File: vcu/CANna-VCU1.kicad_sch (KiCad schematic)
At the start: 12 parts, among them J10 M80-5401042, J11 Conn_01x08_Socket, J12 Conn_01x38_Socket, J13 Conn_01x04_Socket, J14 Conn_01x06_Socket, J3 M80-5401042, J8 M80-5401042, J9 M80-5404242

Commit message: Pfft 3AM changes who knows what this is, probably footprint stuff
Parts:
- J10, J8: footprint (none) -> SUFST:M80-5401042
- J12: footprint (none) -> SUFST:M80-5403842
- J13: footprint (none) -> SUFST:M80-5400442
- J14: footprint (none) -> SUFST:M80-5400642
- J9: footprint (none) -> SUFST:M80-5404242
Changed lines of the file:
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@@
 			)
 		)
-		(property "Footprint" ""
+		(property "Footprint" "SUFST:M80-5404242"
 			(at 177.8 224.79 0)
 			(effects
@@
 			)
 		)
-		(property "Footprint" ""
+		(property "Footprint" "SUFST:M80-5400642"
 			(at 88.9 205.74 0)
 			(effects
@@
 			)
 		)
-		(property "Footprint" ""
+		(property "Footprint" "SUFST:M80-5401042"
 			(at 223.52 189.23 0)
 			(effects
@@
 			)
 		)
-		(property "Footprint" ""
+		(property "Footprint" "SUFST:M80-5401042"
 			(at 53.34 205.74 0)
 			(effects
@@
 			)
 		)
-		(property "Footprint" ""
+		(property "Footprint" "SUFST:M80-5403842"
 			(at 21.59 229.87 0)
 			(effects
@@
 			)
 		)
-		(property "Footprint" ""
+		(property "Footprint" "SUFST:M80-5400442"
 			(at 88.9 248.92 0)
 			(effects

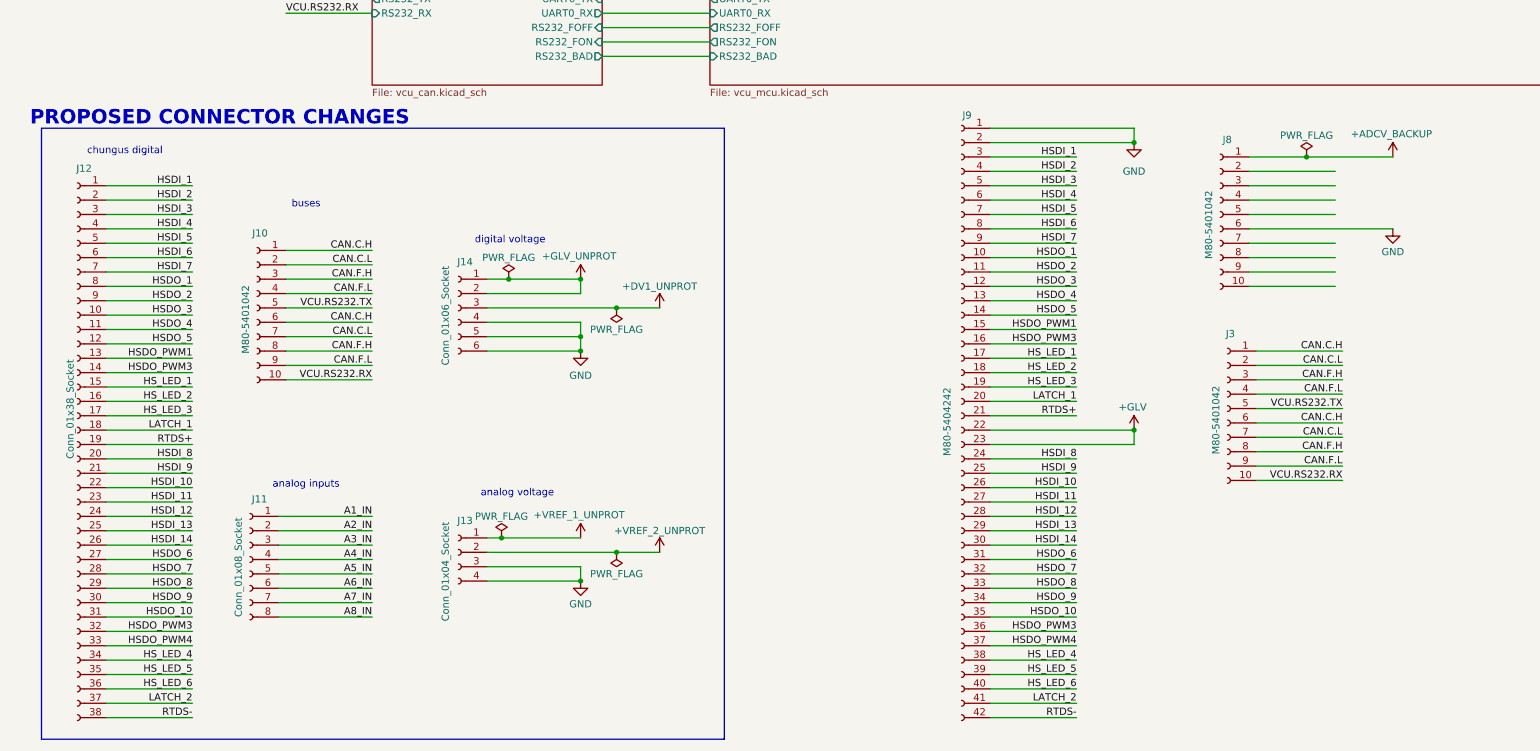
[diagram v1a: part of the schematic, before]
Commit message: fixed connector pinouts
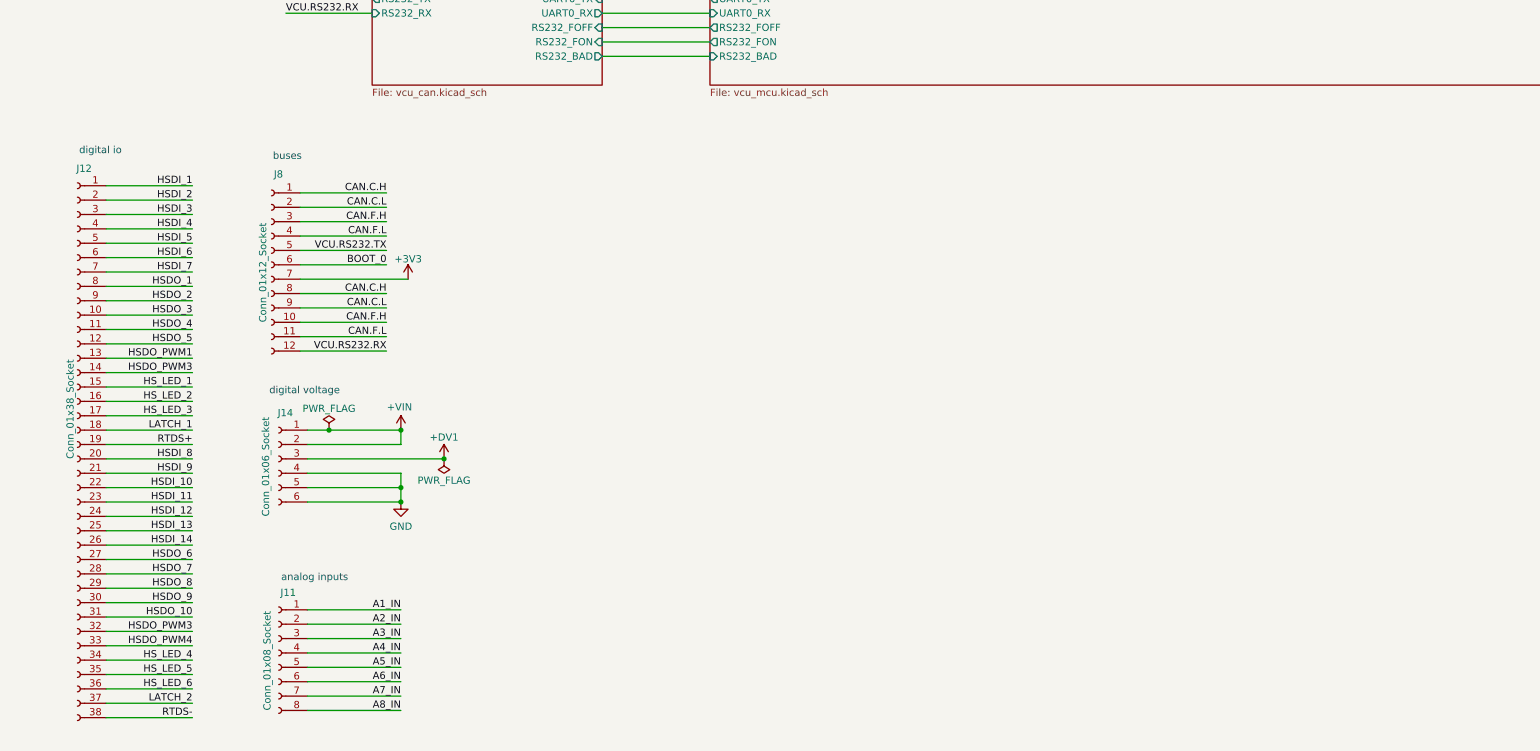
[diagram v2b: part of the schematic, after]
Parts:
- removed J10, J8: M80-5401042, SUFST:M80-5401042, symbol Connector:Conn_01x10_Socket
- removed J13: Conn_01x04_Socket, SUFST:M80-5400442, symbol Connector:Conn_01x04_Socket
- removed J3: M80-5401042, symbol Connector:Conn_01x10_Socket
- removed J9: M80-5404242, SUFST:M80-5404242, symbol Connector:Conn_01x42_Socket
- added J8: Conn_01x12_Socket, symbol Connector:Conn_01x12_Socket
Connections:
- net CAN.C.H: now also J8.1 (Pin_1), J8.8 (Pin_8)
- net CAN.C.L: now also J8.2 (Pin_2), J8.9 (Pin_9)
- net CAN.F.H: now also J8.10 (Pin_10), J8.3 (Pin_3)
- net CAN.F.L: now also J8.11 (Pin_11), J8.4 (Pin_4)
- net VCU.RS232.RX: now also J8.12 (Pin_12)
- net VCU.RS232.TX: now also J8.5 (Pin_5)
- net +DV1_UNPROT renamed +DV1
- net +GLV_UNPROT renamed +VIN
- new net +3V3: J8.7 (Pin_7)
- new net BOOT_0: J8.6 (Pin_6)
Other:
- note added: "digital io"
- note removed: "PROPOSED CONNECTOR CHANGES"
- note removed: "analog voltage"
- note removed: "chungus digital"
- moved on the sheet: J11, J14

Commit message: laying out components
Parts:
- J11: value Conn_01x08_Socket -> M80-5400842; footprint (none) -> SUFST:M80-5400842
- J12: value Conn_01x38_Socket -> M80-5403842
- J14: value Conn_01x06_Socket -> M80-5400642
- J8: value Conn_01x12_Socket -> M80-5401242; footprint (none) -> SUFST:M80-5401242
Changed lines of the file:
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@@
 			)
 		)
-		(property "Value" "Conn_01x12_Socket"
+		(property "Value" "M80-5401242"
 			(at 54.356 208.28 90)
 			(effects
@@
 			)
 		)
-		(property "Footprint" ""
+		(property "Footprint" "SUFST:M80-5401242"
 			(at 55.88 198.12 0)
 			(effects
@@
 			)
 		)
-		(property "Value" "Conn_01x08_Socket"
+		(property "Value" "M80-5400842"
 			(at 55.118 276.86 90)
 			(effects
@@
 			)
 		)
-		(property "Footprint" ""
+		(property "Footprint" "SUFST:M80-5400842"
 			(at 57.15 266.7 0)
 			(effects
@@
 			)
 		)
-		(property "Value" "Conn_01x06_Socket"
+		(property "Value" "M80-5400642"
 			(at 54.864 242.57 90)
 			(effects
@@
 			)
 		)
-		(property "Value" "Conn_01x38_Socket"
+		(property "Value" "M80-5403842"
 			(at 20.32 232.4099 90)
 			(effects

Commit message: layout hell
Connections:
- net HSDO_PWM3: no longer J12.14 (Pin_14)
- new net HSDO_PWM2: J12.14 (Pin_14)

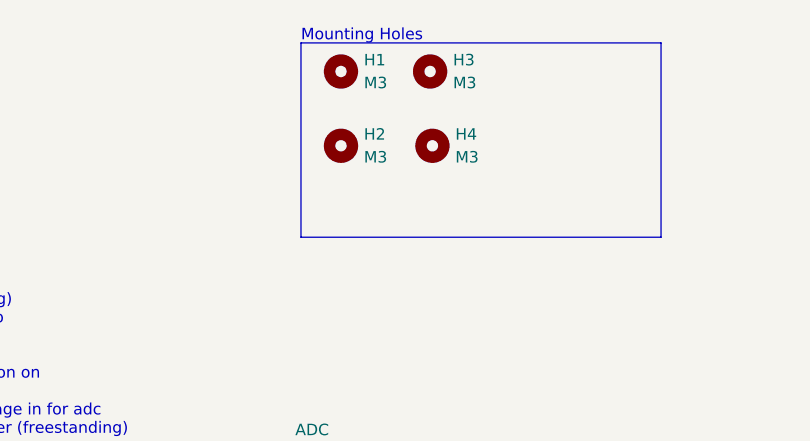
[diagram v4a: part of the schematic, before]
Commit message: added pours
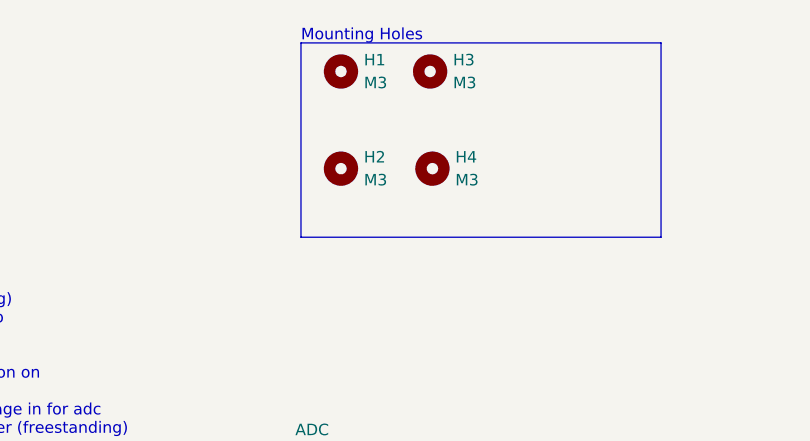
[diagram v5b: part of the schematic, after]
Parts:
- H1, H2, H3, H4: footprint MountingHole:MountingHole_3.2mm_M3 -> MountingHole:MountingHole_3.2mm_M3_DIN965_Pad_TopBottom
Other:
- moved on the sheet: H2, H4
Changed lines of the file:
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@@
 	(symbol
 		(lib_id "Mechanical:MountingHole")
-		(at 88.9 34.29 0)
+		(at 88.9 36.83 0)
 		(unit 1)
 		(exclude_from_sim no)
@@
 		(fields_autoplaced yes)
 		(property "Reference" "H4"
-			(at 91.44 33.0199 0)
+			(at 91.44 35.5599 0)
 			(effects
 				(font
@@
 		)
 		(property "Value" "M3"
-			(at 91.44 35.5599 0)
-			(effects
-				(font
-					(size 1.27 1.27)
-				)
-				(justify left)
-			)
-		)
-		(property "Footprint" "MountingHole:MountingHole_3.2mm_M3"
-			(at 88.9 34.29 0)
+			(at 91.44 38.0999 0)
+			(effects
+				(font
+					(size 1.27 1.27)
+				)
+				(justify left)
+			)
+		)
+		(property "Footprint" "MountingHole:MountingHole_3.2mm_M3_DIN965_Pad_TopBottom"
+			(at 88.9 36.83 0)
 			(effects
 				(font
@@
 		)
 		(property "Datasheet" "~"
-			(at 88.9 34.29 0)
+			(at 88.9 36.83 0)
 			(effects
 				(font
@@
 		)
 		(property "Description" ""
-			(at 88.9 34.29 0)
+			(at 88.9 36.83 0)
 			(effects
 				(font
@@
 		)
 		(property "Optional" "False"
-			(at 88.9 34.29 0)
+			(at 88.9 36.83 0)
 			(effects
 				(font
@@
 	(symbol
 		(lib_id "Mechanical:MountingHole")
-		(at 78.74 34.29 0)
+		(at 78.74 36.83 0)
 		(unit 1)
 		(exclude_from_sim no)
@@
 		(fields_autoplaced yes)
 		(property "Reference" "H2"
-			(at 81.28 33.0199 0)
+			(at 81.28 35.5599 0)
 			(effects
 				(font
@@
 		)
 		(property "Value" "M3"
-			(at 81.28 35.5599 0)
-			(effects
-				(font
-					(size 1.27 1.27)
-				)
-				(justify left)
-			)
-		)
-		(property "Footprint" "MountingHole:MountingHole_3.2mm_M3"
-			(at 78.74 34.29 0)
+			(at 81.28 38.0999 0)
+			(effects
+				(font
+					(size 1.27 1.27)
+				)
+				(justify left)
+			)
+		)
+		(property "Footprint" "MountingHole:MountingHole_3.2mm_M3_DIN965_Pad_TopBottom"
+			(at 78.74 36.83 0)
 			(effects
 				(font
@@
 		)
 		(property "Datasheet" "~"
-			(at 78.74 34.29 0)
+			(at 78.74 36.83 0)
 			(effects
 				(font
@@
 		)
 		(property "Description" ""
-			(at 78.74 34.29 0)
+			(at 78.74 36.83 0)
 			(effects
 				(font
@@
 		)
 		(property "Optional" "False"
-			(at 78.74 34.29 0)
+			(at 78.74 36.83 0)
 			(effects
 				(font
@@
 			)
 		)
-		(property "Footprint" "MountingHole:MountingHole_3.2mm_M3"
+		(property "Footprint" "MountingHole:MountingHole_3.2mm_M3_DIN965_Pad_TopBottom"
 			(at 88.646 26.035 0)
 			(effects
@@
 			)
 		)
-		(property "Footprint" "MountingHole:MountingHole_3.2mm_M3"
+		(property "Footprint" "MountingHole:MountingHole_3.2mm_M3_DIN965_Pad_TopBottom"
 			(at 78.74 26.035 0)
 			(effects

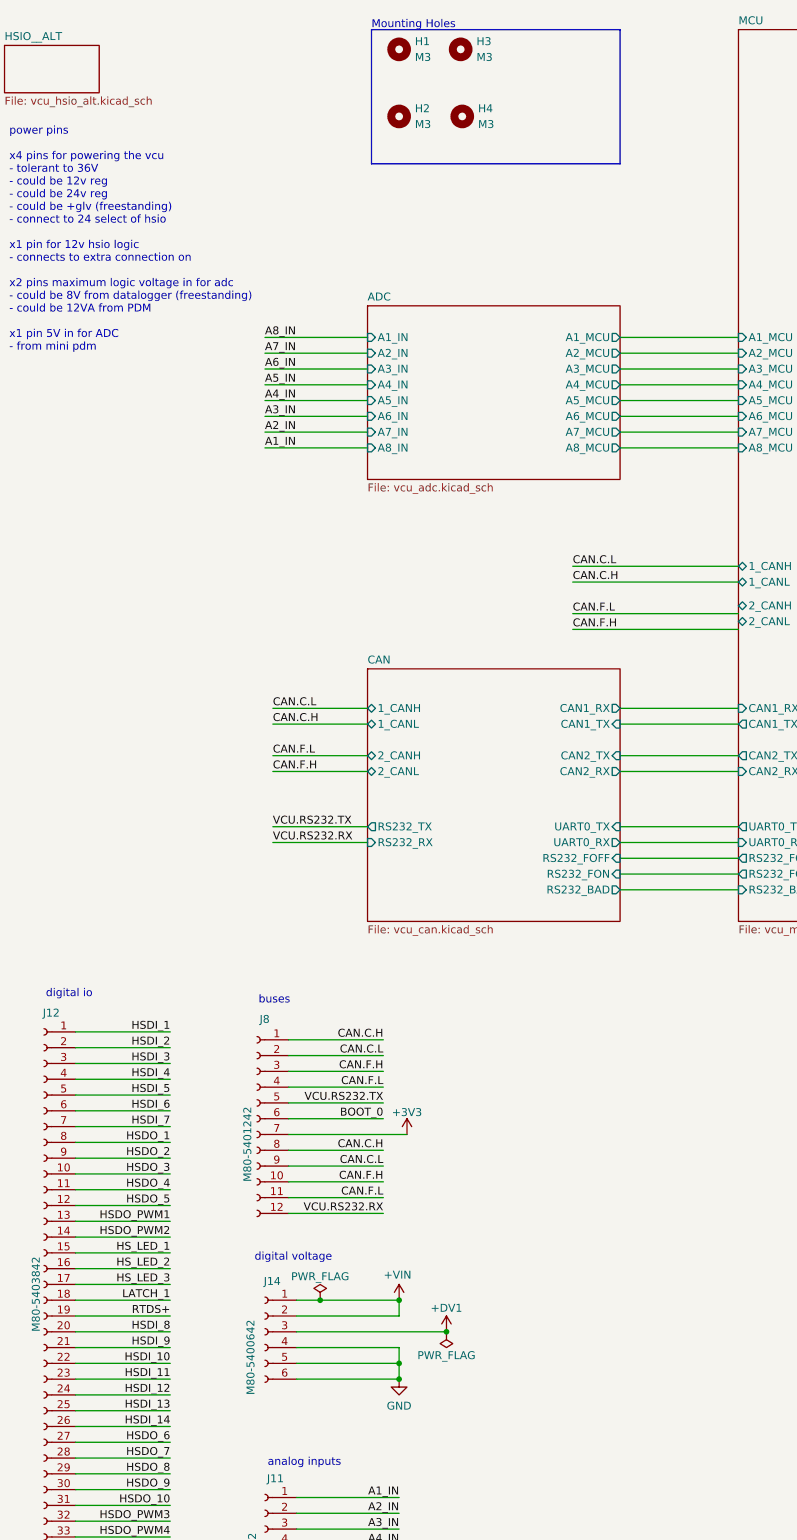
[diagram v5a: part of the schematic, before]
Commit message: filter layout horrors
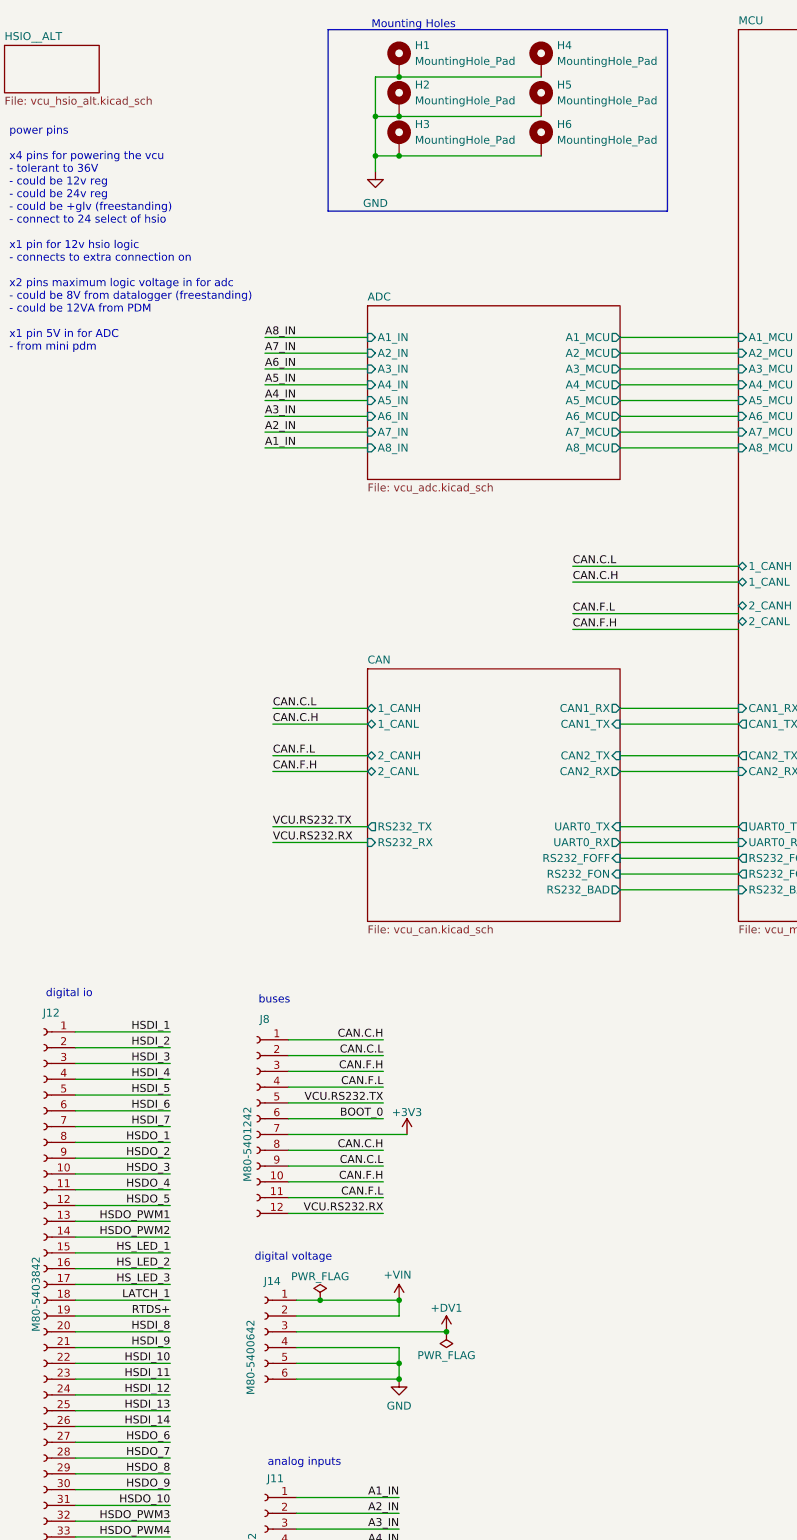
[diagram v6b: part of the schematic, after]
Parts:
- removed H1, H2, H3, H4: M3, MountingHole:MountingHole_3.2mm_M3_DIN965_Pad_TopBottom, symbol Mechanical:MountingHole
- added H1, H2, H3, H4, H5, H6: MountingHole_Pad, MountingHole:MountingHole_3.2mm_M3_DIN965_Pad, symbol Mechanical:MountingHole_Pad
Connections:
- net GND: now also H1.1, H2.1, H3.1, H4.1, H5.1, H6.1
- net HSDI_11: now also J12.23 (Pin_23)
- net HSDI_12: now also J12.24 (Pin_24)
- net HSDI_13: now also J12.25 (Pin_25)
- net HSDI_14: now also J12.26 (Pin_26)
- net HSDI_8: now also J12.20 (Pin_20)
- net HSDI_9: now also J12.21 (Pin_21)

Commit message: tvs spam + some routing
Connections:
- net HSDI_10: now also J12.10 (Pin_10); no longer J12.22 (Pin_22)
- net HSDI_11: now also J12.11 (Pin_11); no longer J12.23 (Pin_23)
- net HSDI_12: now also J12.12 (Pin_12); no longer J12.24 (Pin_24)
- net HSDI_13: now also J12.13 (Pin_13); no longer J12.25 (Pin_25)
- net HSDI_14: now also J12.14 (Pin_14); no longer J12.26 (Pin_26)
- net HSDI_8: now also J12.8 (Pin_8); no longer J12.20 (Pin_20)
- net HSDI_9: now also J12.9 (Pin_9); no longer J12.21 (Pin_21)
- net HSDO_1: now also J12.20 (Pin_20); no longer J12.8 (Pin_8)
- net HSDO_2: now also J12.21 (Pin_21); no longer J12.9 (Pin_9)
- net HSDO_3: now also J12.22 (Pin_22); no longer J12.10 (Pin_10)
- net HSDO_4: now also J12.23 (Pin_23); no longer J12.11 (Pin_11)
- net HSDO_5: now also J12.24 (Pin_24); no longer J12.12 (Pin_12)
- net HSDO_PWM1: now also J12.25 (Pin_25); no longer J12.13 (Pin_13)
- net HSDO_PWM2: now also J12.26 (Pin_26); no longer J12.14 (Pin_14)

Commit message: routing routing routing PLEASE DO NOT TOUCH
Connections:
- net +3V3: now also J8.8 (Pin_8); no longer J8.7 (Pin_7)
- net +DV1: now also J14.1 (Pin_1); no longer J14.3 (Pin_3)
- net +VIN: now also J14.3 (Pin_3); no longer J14.1 (Pin_1)
- net BOOT_0: now also J8.2 (Pin_2); no longer J8.6 (Pin_6)
- net CAN.C.H: now also J8.12 (Pin_12), J8.6 (Pin_6); no longer J8.1 (Pin_1), J8.8 (Pin_8)
- net CAN.C.L: now also J8.11 (Pin_11), J8.5 (Pin_5); no longer J8.2 (Pin_2), J8.9 (Pin_9)
- net CAN.F.H: now also J8.4 (Pin_4); no longer J8.3 (Pin_3)
- net CAN.F.L: now also J8.3 (Pin_3), J8.9 (Pin_9); no longer J8.11 (Pin_11), J8.4 (Pin_4)
- net VCU.RS232.RX: now also J8.1 (Pin_1); no longer J8.12 (Pin_12)
- net VCU.RS232.TX: now also J8.7 (Pin_7); no longer J8.5 (Pin_5)
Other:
- note added: "power"
- note removed: "digital voltage"
